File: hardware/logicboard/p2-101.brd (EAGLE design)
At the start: 72 x 72 mm, 67 parts, among them IC1 74LS06N, IC11 74LS153D, IC12 LTC485S, IC13 LTC485S, IC2 4066N, J1 MKR, J11 Qwiic, J12 Qwiic, J13 Qwiic, J14 Qwiic, J2 GPIO, J3 Vcc, J4 RLY, J5 SPI, J6 LED, K1 G5V1, T1 2SC1815, U1 DS18B20

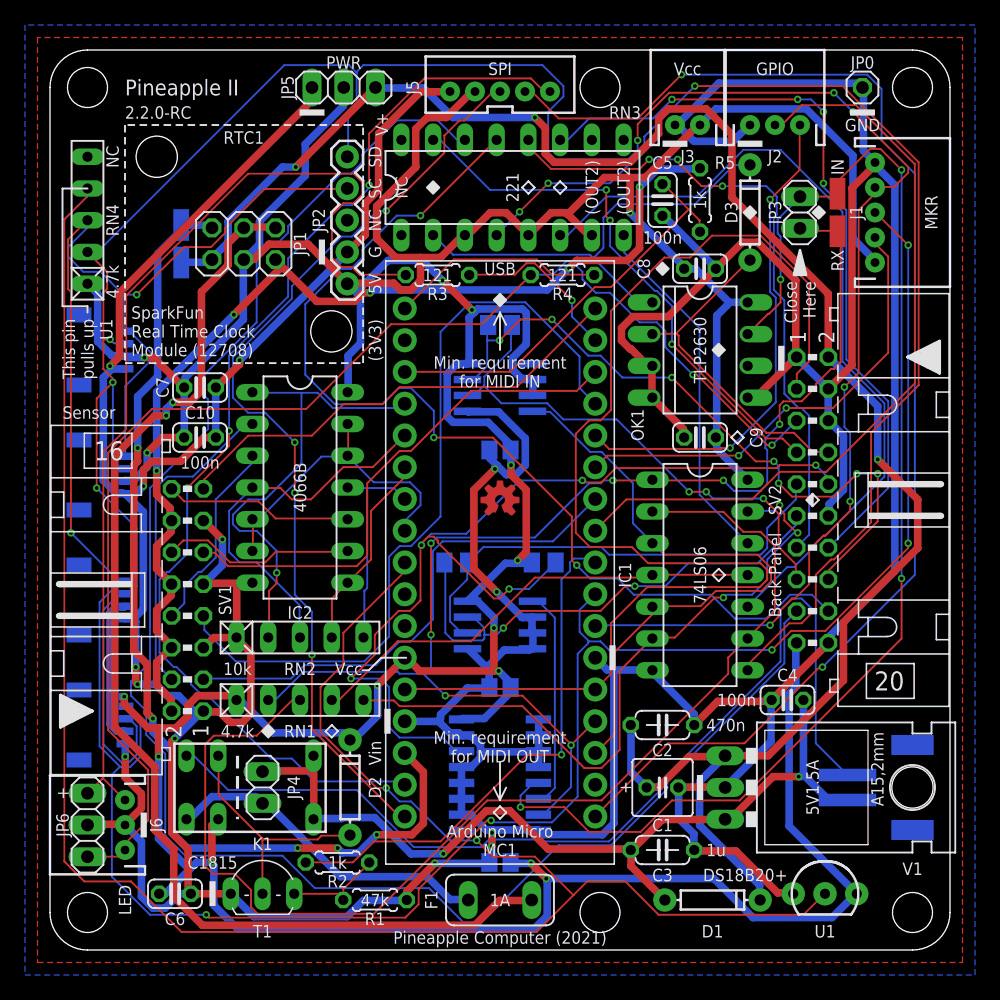
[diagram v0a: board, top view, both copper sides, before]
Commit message: Removed Arduino.
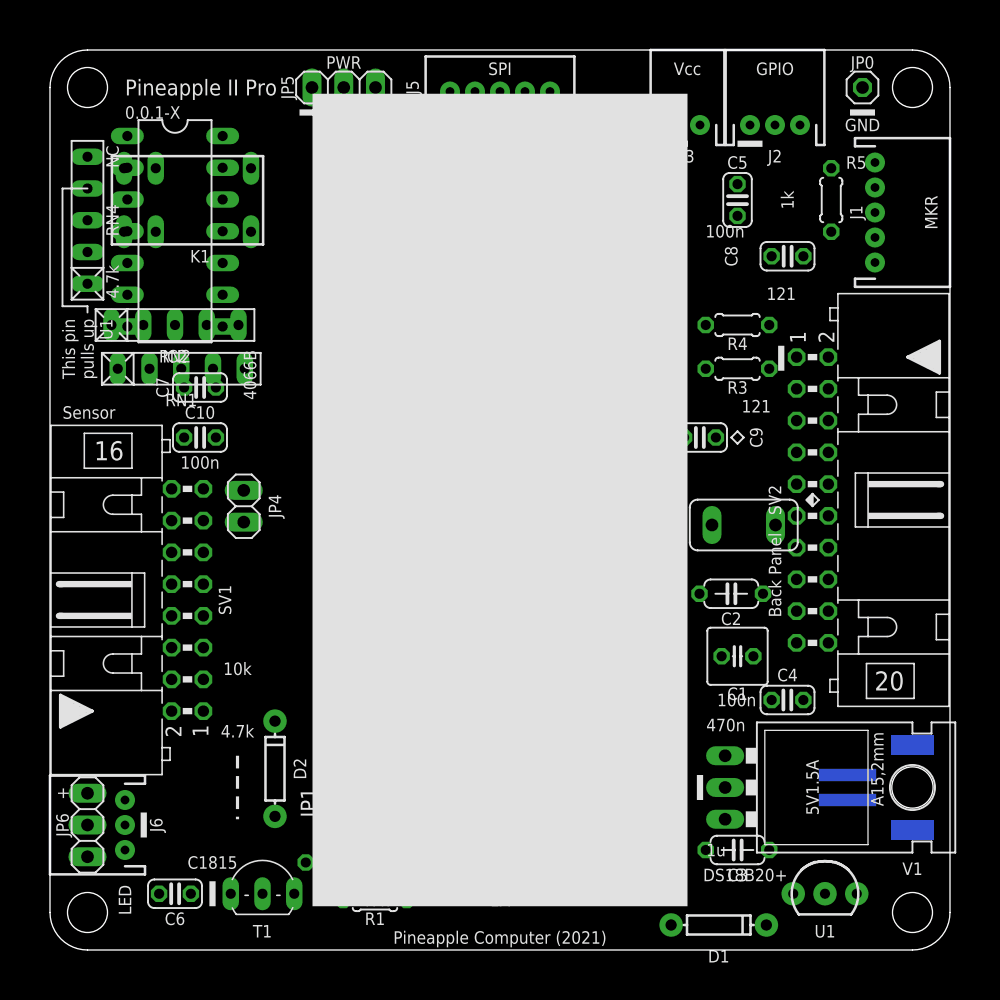
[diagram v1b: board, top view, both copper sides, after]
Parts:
- removed C11, C12, C13: 10n, rcl:C2012
- removed D3: (no value), SparkFun-DiscreteSemi:DIODE-1N4148
- removed H1, H2: STAND-OFF, SparkFun-Hardware:STAND-OFF
- removed IC1: 74LS06N, 74xx-us:DIL14
- removed IC11: 74LS153D, 74xx-us:SO16
- removed IC12, IC13: LTC485S, linear-technology:SOIC8
- removed IN, RX, V+, VIN: (no value), wirepad:SMD1,27-2,54
- removed J11, J12, J13, J14: Qwiic, SparkFun-Connectors:1X04_1MM_RA
- removed JP2: RTC, SparkFun-Connectors:1X05
- removed JP3: MPXJMP, pinhead:1X02
- removed MC1: ARDUINOMICRO, adafruit:ARDUINOMICRO
- removed OK1: HCPL2630, optocoupler:DIL08
- removed R11: 10k, rcl:M2012
- removed R12, R13: 120, rcl:M2012
- removed RN3: 220, resistor-dil:DIL16
- JP1: value PWRSEL -> (none); device pinhead:2X03 -> pinhead:2X20
- moved K1 47.3 mm to (11.0, 60.0)
- moved F1 35.8 mm to (55.5, 34.0)
- moved RN1 28.2 mm to (10.5, 46.5)
- moved RN2 26.9 mm to (10.0, 50.0)
- moved R3 25.1 mm to (55.0, 46.5)
- moved IC2 22.8 mm to (10.0, 57.5)
- moved JP4 22.5 mm to (15.5, 35.5)
- moved JP1 22.4 mm to (24.5, 36.0), turned to 90 degrees
- moved R4 14.6 mm to (55.0, 50.0)
- moved C1 12.1 mm to (55.0, 23.5)
- moved C2 11.9 mm to (54.5, 28.5)
- moved R5 10.5 mm to (62.5, 60.0)
- moved C8 7.07 mm to (59.0, 55.5)
- moved D2 6.18 mm to (18.0, 14.5)
- moved C3 6.00 mm to (55.0, 8.00)
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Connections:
- removed net MIDIINSND: D3.C, OK1.1, RN3.2
- removed net MIN: IC11.5, IN.1, JP3.2, OK1.7
- removed net MO2RTN: RN3.9
- removed net MO2RTNRAW: IC1.12, RN3.8
- removed net MO2SND: RN3.10
- removed net MORTNRAW: IC1.10, RN3.6
- removed net MRX: IC11.6, IC12.1
- removed net MTRTNRAW: IC1.8, RN3.4
- removed net TX: IC1.3, IC1.5, IC13.4, MC1.P$15
- removed net VDD: MC1.P$33
- removed net VIN: JP1.2, MC1.P$20, VIN.1
- net ANLG1: no longer MC1.P$31
- net ANLG2: no longer MC1.P$30
- net ANLG3: no longer MC1.P$29
- net ANLG4: no longer MC1.P$28
- net AREF: no longer MC1.P$32
- net D7: no longer MC1.P$6
- net DTCT1: no longer MC1.P$7
- net DTCT2: no longer MC1.P$4
- net DTCT3: no longer MC1.P$3
- net DTCT4: no longer MC1.P$1
- net GATE: no longer MC1.P$27
- net GND: no longer C11.2, C12.2, C13.2, IC1.7, IC11.1, IC11.10, IC11.11, IC11.12, IC11.13, IC11.15, IC11.2, IC11.3, IC11.4, IC11.8, IC12.2, IC12.3, IC12.4, IC12.5, IC13.5, J11.1, J12.1, J13.1, J14.1, JP2.2, MC1.P$12, MC1.P$21, OK1.3, OK1.4, OK1.5
- net GPIO1: no longer MC1.P$8
- net GPIO2: no longer MC1.P$5
- net LED0: no longer MC1.P$34
- net LED1: no longer MC1.P$2
- net MIRTN: no longer D3.A, OK1.2
- net MISND: no longer RN3.15
- net MISO: no longer MC1.P$19
- net MORTN: no longer RN3.11
- net MOSI: no longer MC1.P$17
- net MOSND: no longer RN3.12
- net MRX+: no longer IC12.6, R12.1
- net MRX-: no longer IC12.7, R12.2
- net MRXDTCT: no longer IC11.14, R11.1
- net MTRTN: no longer RN3.13
- net MTSND: no longer RN3.14
- net MTX+: no longer IC13.6, R13.1
- net MTX-: no longer IC13.7, R13.2
- net NMO2RTN: no longer IC1.13, IC1.6
- net NMORTN: no longer IC1.11, IC1.4
- net NMTRTN: no longer IC1.2, IC1.9
- net RLY: no longer MC1.P$9
- net RST: no longer MC1.P$13, MC1.P$22
- net RX: no longer IC1.1, IC11.7, JP3.1, MC1.P$14, RX.1
- net SCK: no longer MC1.P$18
- net SCL: no longer J11.4, J12.4, J13.4, J14.4, JP2.4, MC1.P$10
- net SDA: no longer J11.3, J12.3, J13.3, J14.3, JP2.5, MC1.P$11
- net THS: no longer MC1.P$26
- net V+: no longer JP1.1, V+.1
- net VCC: no longer C11.1, C12.1, C13.1, IC1.14, IC11.16, IC12.8, IC13.2, IC13.3, IC13.8, J11.2, J12.2, J13.2, J14.2, JP1.3, JP2.1, MC1.P$23, OK1.8, R11.2, RN3.3, RN3.5, RN3.7
- net VCC/2: no longer JP1.5
- net VOUT: no longer JP1.4, JP1.6
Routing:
- net GND: track 503.7 -> 0.00 mm, vias 13 -> 0
- net VCC: track 418.6 -> 0.00 mm, vias 15 -> 0
- net SCL: track 227.9 -> 0.00 mm, vias 7 -> 0
- net SDA: track 210.3 -> 0.00 mm, vias 9 -> 0
- net THS: track 163.2 -> 0.00 mm, vias 2 -> 0
- net V+: track 149.4 -> 0.00 mm, vias 3 -> 0
- net MTSND: track 140.2 -> 0.00 mm
- net LED0A: track 106.5 -> 0.00 mm, vias 2 -> 0
- net MOSI: track 104.9 -> 0.00 mm, vias 2 -> 0
- net RX: track 104.5 -> 0.00 mm, vias 7 -> 0
- net MIN: track 101.9 -> 0.00 mm, vias 4 -> 0
- net RST: track 100.5 -> 0.00 mm
- net VOUT: track 94.1 -> 0.00 mm, vias 2 -> 0
- net NMTRTN: track 93.7 -> 0.00 mm
- net MISO: track 89.9 -> 0.00 mm, vias 3 -> 0
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- removed copper zone on layer 1, net GND
- removed copper zone on layer 16, net GND
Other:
- board text added: "0.0.1-X"
- board text added: "Pineapple II Pro"
- board text removed: "(3V3)"
- board text removed: "(OUT2)"
- board text removed: "2.2.0-RC"
- board text removed: "221"
- board text removed: "5V"
- board text removed: "74LS06"
- board text removed: "Arduino Micro"
- board text removed: "Close Here"
- board text removed: "MC1"
- board text removed: "Min. requirement for MIDI IN"
- board text removed: "Min. requirement for MIDI OUT"
- board text removed: "Pineapple II"
- board text removed: "RTC1"
- board text removed: "SparkFun Real Time Clock Module (12708)"
- board text removed: "TLP2630"
- board text removed: "USB"

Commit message: Unknown...
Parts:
- removed C10, C4, C5: 100n, rcl:C025-024X044
- removed C3: 1u, rcl:C050-024X044
- removed C6, C7, C8, C9: 10n, resistor:C025-024X044
- removed D1, D2: (no value), SparkFun-DiscreteSemi:DIODE-1N4148
- removed F1: 1.8A, fuse:TE5
- removed J4: RLY, SparkFun-Connectors:JST-2-SMD
- removed J6: LED, SparkFun-Connectors:JST-3-PTH
- removed JP0: GNDPIN, pinhead:1X01
- removed JP4: RLYJMP, pinhead:1X02
- removed JP5: D5V, pinhead:1X03
- removed JP6: LED, pinhead:1X03
- removed K1: G5V1, relay:G5V1
- removed RN1, RN4: 4.7k, resistor-net:RN-5
- removed RN2: 10k, resistor-net:RN-5
- removed SV2: (no value), con-ml:ML20L
- removed T1: 2SC1815, transistor:TO92-ECB
- removed V1: 5V, v-reg:78XXL
- added R6, R7, R8: (no value), rcl:M2012
- C1: value 22u -> (none); device rcl:C025-050X050 -> rcl:C2012
- C2: value 470n -> (none); device rcl:C050-024X044 -> rcl:C2012
- IC2: value 4066N -> 4066D; device 40xx:DIL14 -> 40xx:SO14
- R1: value 47k -> (none); device resistor:0204/5 -> rcl:M2012
- R2, R5: value 1k -> (none); device resistor:0204/5 -> rcl:M2012
- R3, R4: value 120 -> (none); device resistor:0204/5 -> rcl:M2012
- moved R5 65.3 mm to (23.0, 8.00), turned to 0 degrees
- moved J5 62.6 mm to (3.50, 15.0), turned to 90 degrees
- moved J3 55.6 mm to (59.0, 11.0), turned to 270 degrees
- moved U1 55.5 mm to (11.0, 26.5), turned to 180 degrees
- moved R3 55.5 mm to (15.0, 8.00)
- moved R4 55.3 mm to (19.0, 8.00)
- moved J2 48.0 mm to (59.0, 18.0), turned to 270 degrees
- moved IC2 42.6 mm to (13.0, 15.0), turned to 0 degrees
- moved J1 37.5 mm to (52.5, 24.0), turned to 0 degrees
- moved C1 37.0 mm to (19.0, 15.0), turned to 90 degrees
- moved JP1 33.5 mm to (32.5, 3.50), turned to 180 degrees
- moved LOGO1 28.7 mm to (11.0, 22.0)
- moved C2 25.7 mm to (39.0, 8.00)
- moved SV1 23.3 mm to (32.5, 19.0), turned to 0 degrees
- moved U$1 22.8 mm to (32.5, 11.0), flipped to the top
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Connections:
- removed net LED0: R4.2
- removed net LED0A: J6.1, JP6.1, R4.1, SV2.5
- removed net LED1: R3.2
- removed net LED1A: J6.3, JP6.3, R3.1
- removed net MIRTN: SV2.8
- removed net MISND: SV2.7
- removed net MORTN: SV2.14
- removed net MOSND: SV2.13
- removed net MRX+: SV2.9
- removed net MRX-: SV2.11
- removed net MRXDTCT: SV2.10
- removed net MTRTN: SV2.18
- removed net MTSND: SV2.17
- removed net MTX+: SV2.15
- removed net MTX-: SV2.16
- removed net NMO2RTN: RN1.5
- removed net NMORTN: RN1.4
- removed net NMTRTN: RN1.3
- removed net RLY: R2.2
- removed net RLYDRV: R1.2, R2.1, T1.B
- removed net RLYOUT: J4.2, K1.10
- removed net RLYSNK: D2.A, K1.9, T1.C
- removed net RST: SV2.3
- removed net V+: C1.1, C2.1, D1.C, JP5.3, SV2.2, V1.IN
- removed net VOUT: F1.2
- removed net VOUTRAW: C3.1, C4.1, D1.A, J4.1, JP4.2, K1.5, K1.6, V1.OUT
- removed net VOUTRAW2: F1.1, JP4.1, K1.1
- new net CE0: JP1.24
- new net CE1: JP1.26
- new net EEPROMSCL: JP1.28
- new net EEPROMSDA: JP1.27
- new net GPCLK0: JP1.7
- new net GPIO16: JP1.36
- new net GPIO17: JP1.11
- new net GPIO22: JP1.15
- new net GPIO23: JP1.16
- new net GPIO24: JP1.18
- new net GPIO25: JP1.22
- new net GPIO26: JP1.37
- new net GPIO27: JP1.13
- new net GPIO5: JP1.29
- new net GPIO6: JP1.31
- new net MISO0: JP1.21
- new net MOSI0: JP1.19
- new net PCMCLK: JP1.12
- new net PCMDIN: JP1.38
- new net PCMDOUT: JP1.40
- new net PCMFS: JP1.35
- new net PWM0: JP1.32
- new net PWM1: JP1.33
- new net SCL1: JP1.5
- new net SCLK0: JP1.23
- new net SDA1: JP1.3
- new net TX: JP1.8
- new net VDD: JP1.1, JP1.17
- net ANLG1: now also R1.2; no longer RN2.2
- net ANLG2: now also R2.2; no longer RN2.3
- net ANLG3: now also R3.2; no longer RN2.4
- net ANLG4: now also R4.2; no longer RN2.5
- net AREF: now also C2.1, R8.2; no longer C5.1, R5.1
- net GND: now also JP1.14, JP1.20, JP1.25, JP1.30, JP1.34, JP1.39, JP1.6, JP1.9, R2.1, R3.1, R4.1; no longer C10.2, C3.2, C4.2, C5.2, C6.2, C7.2, C8.2, C9.2, J6.2, JP0.1, JP5.1, JP6.2, RN2.1, SV2.1, SV2.12, SV2.20, SV2.4, SV2.6, T1.E, V1.GND
- net RX: now also JP1.10; no longer RN1.2
- net SCL: now also R6.2; no longer RN4.3
- net SDA: now also R5.2; no longer RN4.2
- net THS: now also R7.2; no longer RN4.4
- net VCC: now also C1.1, JP1.2, JP1.4, R5.1, R6.1, R7.1, R8.1; no longer C10.1, C6.1, C7.1, C8.1, C9.1, D2.C, JP5.2, K1.2, RN1.1, RN4.1, SV2.19
- net VCC/2: no longer R5.2
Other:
- board size 72 x 72 mm -> 65 x 30 mm
- board text removed: "*Cut pull-up R to install LM35"
- board text removed: "*Cut this pin to use LM35"
- board text removed: "+"
- board text removed: "0.0.1-X"
- board text removed: "100n"
- board text removed: "10k"
- board text removed: "121"
- board text removed: "1A"
- board text removed: "1k"
- board text removed: "1u"
- board text removed: "3V3"
- board text removed: "4.7k"
- board text removed: "4066B"
- board text removed: "470n"
- board text removed: "47k"
- board text removed: "5V1.5A"
- board text removed: "74153"
- board text removed: "Arduino"
- board text removed: "Back Panel"
- board text removed: "Bottom View"
- board text removed: "C"
- board text removed: "C1815"
- board text removed: "Close"
- board text removed: "D7"
- board text removed: "DS18B20+"
- board text removed: "Direct 5V"
- board text removed: "Don't Close"
- board text removed: "Dual"
- board text removed: "Ext. V+"
- board text removed: "G"
- board text removed: "G1"
- board text removed: "G2"
- board text removed: "GND"
- board text removed: "GPIO"
- board text removed: "I"
- board text removed: "IN-RX"
- board text removed: "Insulating Tape Here"
- board text removed: "LED"
- board text removed: "LED0"
- board text removed: "LED1"
- board text removed: "LTC485"
- board text removed: "MKR"
- board text removed: "NC"
- board text removed: "O"
- board text removed: "OUT2"
- board text removed: "Open JP1"
- board text removed: "PWR"
- board text removed: "PWRSEL"
- board text removed: "Pineapple Computer (2021)"
- board text removed: "Qwiic/5V"
- board text removed: "RLYJMP"
- board text removed: "RTN"
- board text removed: "RX"
- board text removed: "Regulator"
- board text removed: "Relay"
- board text removed: "SC"
- board text removed: "SCL"
- board text removed: "SD"
- board text removed: "SDA"
- board text removed: "SND"
- board text removed: "SPI"
- board text removed: "Sensor"
- board text removed: "TX"
- board text removed: "This pin pulls up U1"
- board text removed: "U1"
- board text removed: "V"
- board text removed: "V+"
- board text removed: "Vcc"
- board text removed: "Vcc/2"
- board text removed: "Vin"
- board text removed: "Vin (MC)"
- board text removed: "Vout"
- board text removed: "Vout (Reg)"
- board text removed: "Voutraw"
- board text removed: "You can istall LM35* instead of DS18B20+"
